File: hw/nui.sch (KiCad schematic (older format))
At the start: 20 parts, among them J1 D_PWR, J2 IR_RCV, J3 A_PWR, J4 Input, J5 Output, U1 Teensy-LC, U2 TC7660S, U3 PGA2311

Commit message: Footprints assigned and created
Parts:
- D1, D2: footprint (none) -> alvarop:SP1002-02JTG
- J4, J5: footprint (none) -> alvarop:SJ-3524-SMT-TR
- U1: footprint (none) -> alvarop:Teensy-LC
- U2: footprint (none) -> alvarop:TC7660S-SOIC
- U3: footprint (none) -> alvarop:PGA2311-SOIC
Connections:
- no-connect marks 19 -> 21
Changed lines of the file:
@@
 LIBS:valves
 LIBS:alvarop
-LIBS:teensy
 LIBS:nui-cache
 EELAYER 25 0
@@
 F 0 "U2" H 8450 2300 60  0000 C CNN
 F 1 "TC7660S" H 8450 1800 60  0000 C CNN
-F 2 "" H 8450 2050 60  0001 C CNN
+F 2 "alvarop:TC7660S-SOIC" H 8450 2050 60  0001 C CNN
 F 3 "" H 8450 2050 60  0001 C CNN
 F 4 " TC7660SEOA713" H 8450 2050 60  0001 C CNN "MPN"
@@
 F 0 "U3" H 8450 4600 60  0000 C CNN
 F 1 "PGA2311" H 8450 3700 60  0000 C CNN
-F 2 "" H 8450 4150 60  0001 C CNN
+F 2 "alvarop:PGA2311-SOIC" H 8450 4150 60  0001 C CNN
 F 3 "" H 8450 4150 60  0001 C CNN
 F 4 "PGA2311U" H 8450 4150 60  0001 C CNN "MPN"
@@
 F 0 "J5" H 8750 5190 50  0000 C CNN
 F 1 "Output" H 8600 4800 50  0000 L CNN
-F 2 "" H 9000 5100 50  0001 C CNN
+F 2 "alvarop:SJ-3524-SMT-TR" H 9000 5100 50  0001 C CNN
 F 3 "" H 9000 5100 50  0001 C CNN
 F 4 " SJ-3524-SMT-TR" H 8750 5000 60  0001 C CNN "MPN"
@@
 	7150 3200 7150 3150
 Wire Wire Line
-	7150 3150 7450 3150
-Wire Wire Line
-	7450 3150 7650 3150
+	7150 3150 7650 3150
 Wire Wire Line
 	7450 3200 7450 3150
@@
 	7150 3400 7150 3450
 Wire Wire Line
-	7150 3450 7450 3450
-Wire Wire Line
-	7450 3450 7650 3450
+	7150 3450 7650 3450
 Wire Wire Line
 	7450 3400 7450 3450
@@
 	8150 3200 8150 3150
 Wire Wire Line
-	8150 3150 8450 3150
-Wire Wire Line
-	8450 3150 8650 3150
+	8150 3150 8650 3150
 Wire Wire Line
 	8450 3200 8450 3150
@@
 	8150 3400 8150 3450
 Wire Wire Line
-	8150 3450 8450 3450
-Wire Wire Line
-	8450 3450 8650 3450
+	8150 3450 8650 3450
 Wire Wire Line
 	8450 3400 8450 3450
@@
 	9100 3200 9100 3150
 Wire Wire Line
-	9100 3150 9400 3150
-Wire Wire Line
-	9400 3150 9600 3150
+	9100 3150 9600 3150
 Wire Wire Line
 	9400 3200 9400 3150
@@
 	9100 3400 9100 3450
 Wire Wire Line
-	9100 3450 9400 3450
-Wire Wire Line
-	9400 3450 9600 3450
+	9100 3450 9600 3450
 Wire Wire Line
 	9400 3400 9400 3450
 Connection ~ 9400 3450
 Wire Wire Line
-	8800 1900 8850 1900
-Wire Wire Line
-	8850 1900 9000 1900
-Wire Wire Line
-	9000 1900 9200 1900
-Wire Wire Line
-	9200 1900 9450 1900
+	8800 1900 9450 1900
 Wire Wire Line
 	8850 1900 8850 1650
@@
 Connection ~ 8850 1900
 Wire Wire Line
-	8800 2200 9000 2200
-Wire Wire Line
-	9000 2200 9200 2200
-Wire Wire Line
-	9200 2200 9450 2200
+	8800 2200 9450 2200
 Wire Wire Line
 	7200 1950 7200 1900
 Wire Wire Line
-	7200 1900 7400 1900
-Wire Wire Line
-	7400 1900 7950 1900
+	7200 1900 7950 1900
 Wire Wire Line
 	7950 1900 7950 2000
@@
 Connection ~ 7400 1900
 Wire Wire Line
-	7200 2200 7400 2200
-Wire Wire Line
-	7400 2200 7500 2200
+	7200 2200 7500 2200
 Wire Wire Line
 	7400 2200 7400 2150
@@
 Wire Wire Line
 	3500 2750 3350 2750
-Wire Wire Line
-	3500 2650 3350 2650
-Wire Wire Line
-	3500 2550 3350 2550
 Text Label 3350 2850 2    60   ~ 0
 MUTE_N
@@
 $EndComp
 Wire Wire Line
-	8550 5200 8550 5350
-Wire Wire Line
-	8550 5350 8550 5450
-Wire Wire Line
-	8550 5450 8550 5550
-Wire Wire Line
-	8950 5100 9350 5100
-Wire Wire Line
-	9350 5100 9450 5100
-Wire Wire Line
-	8950 4900 9250 4900
-Wire Wire Line
-	9250 4900 9450 4900
+	8550 5200 8550 5550
+Wire Wire Line
+	8950 5100 9450 5100
+Wire Wire Line
+	8950 4900 9450 4900
 Text Label 8050 5100 0    60   ~ 0
 VIN_L
@@
 F 0 "D2" H 9000 5550 60  0000 C CNN
 F 1 "SP1002-02JTG" H 9000 5240 60  0000 C CNN
-F 2 "" H 8880 5230 60  0001 C CNN
+F 2 "alvarop:SP1002-02JTG" H 8880 5230 60  0001 C CNN
 F 3 "" H 8880 5230 60  0001 C CNN
 F 4 " SP1002-02JTG" H 9000 5400 60  0001 C CNN "MPN"
@@
 F 0 "J4" H 7350 5190 50  0000 C CNN
 F 1 "Input" H 7200 4800 50  0000 L CNN
-F 2 "" H 7600 5100 50  0001 C CNN
+F 2 "alvarop:SJ-3524-SMT-TR" H 7600 5100 50  0001 C CNN
 F 3 "" H 7600 5100 50  0001 C CNN
 F 4 " SJ-3524-SMT-TR" H 7350 5000 60  0001 C CNN "MPN"
@@
 $EndComp
 Wire Wire Line
-	7150 5200 7150 5350
-Wire Wire Line
-	7150 5350 7150 5450
-Wire Wire Line
-	7150 5450 7150 5550
-Wire Wire Line
-	7550 5100 7950 5100
-Wire Wire Line
-	7950 5100 8050 5100
-Wire Wire Line
-	7550 4900 7850 4900
-Wire Wire Line
-	7850 4900 8050 4900
+	7150 5200 7150 5550
+Wire Wire Line
+	7550 5100 8050 5100
+Wire Wire Line
+	7550 4900 8050 4900
 NoConn ~ 7550 5000
 Wire Wire Line
@@
 F 0 "D1" H 7600 5550 60  0000 C CNN
 F 1 "SP1002-02JTG" H 7600 5240 60  0000 C CNN
-F 2 "" H 7480 5230 60  0001 C CNN
+F 2 "alvarop:SP1002-02JTG" H 7480 5230 60  0001 C CNN
 F 3 "" H 7480 5230 60  0001 C CNN
 F 4 " SP1002-02JTG" H 7600 5400 60  0001 C CNN "MPN"
@@
 F 0 "U1" H 4550 3650 60  0000 C CNN
 F 1 "Teensy-LC" H 4550 1650 60  0000 C CNN
-F 2 "" H 4550 1950 60  0001 C CNN
+F 2 "alvarop:Teensy-LC" H 4550 1950 60  0001 C CNN
 F 3 "" H 4550 1950 60  0000 C CNN
 F 4 "TEENSYLC" H 4550 2500 60  0001 C CNN "MPN"
@@
 $EndComp
 NoConn ~ 5650 2550
+NoConn ~ 3500 2550
+NoConn ~ 3500 2650
+$Comp
+L PWR_FLAG #FLG020
+U 1 1 5A4A9E01
+P 3650 6700
+F 0 "#FLG020" H 3650 6775 50  0001 C CNN
+F 1 "PWR_FLAG" H 3650 6850 50  0000 C CNN
+F 2 "" H 3650 6700 50  0001 C CNN
+F 3 "" H 3650 6700 50  0001 C CNN
+	1    3650 6700
+	1    0    0    -1
+$EndComp
+Connection ~ 3650 6700
+$Comp
+L PWR_FLAG #FLG021
+U 1 1 5A4A9ED3
+P 4650 6750
+F 0 "#FLG021" H 4650 6825 50  0001 C CNN
+F 1 "PWR_FLAG" H 4650 6900 50  0000 C CNN
+F 2 "" H 4650 6750 50  0001 C CNN
+F 3 "" H 4650 6750 50  0001 C CNN
+	1    4650 6750
+	1    0    0    -1
+$EndComp
+$Comp
+L PWR_FLAG #FLG022
+U 1 1 5A4A9F42
+P 5750 6750
+F 0 "#FLG022" H 5750 6825 50  0001 C CNN
+F 1 "PWR_FLAG" H 5750 6900 50  0000 C CNN
+F 2 "" H 5750 6750 50  0001 C CNN
+F 3 "" H 5750 6750 50  0001 C CNN
+	1    5750 6750
+	1    0    0    -1
+$EndComp
+$Comp
+L PWR_FLAG #FLG023
+U 1 1 5A4A9F89
+P 5750 6950
+F 0 "#FLG023" H 5750 7025 50  0001 C CNN
+F 1 "PWR_FLAG" H 5750 7100 50  0000 C CNN
+F 2 "" H 5750 6950 50  0001 C CNN
+F 3 "" H 5750 6950 50  0001 C CNN
+	1    5750 6950
+	-1   0    0    1
+$EndComp
+Connection ~ 4650 6750
+Connection ~ 5750 6750
+Connection ~ 5750 6950
+$Comp
+L PWR_FLAG #FLG?
+U 1 1 5A4AA207
+P 6000 2050
+F 0 "#FLG?" H 6000 2125 50  0001 C CNN
+F 1 "PWR_FLAG" H 6000 2200 50  0000 C CNN
+F 2 "" H 6000 2050 50  0001 C CNN
+F 3 "" H 6000 2050 50  0001 C CNN
+	1    6000 2050
+	-1   0    0    1
+$EndComp
+Connection ~ 6000 2050
 $EndSCHEMATC

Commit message: Layout almost done
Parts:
- removed C2, C7: DNP, Capacitors_Tantalum_SMD:CP_Tantalum_Case-A_EIA-3216-18_Reflow, symbol CP1_Small
- added R1, R2: 0, Capacitors_SMD:C_0603, symbol R_Small
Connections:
- net GNDA: now also C9.1, R1.1; no longer C1.2, C4.2, J1.2 (Pin_2), J2.3 (Pin_3), U1.1 (GND), U1.27 (GND), U3.5 (DGND)
- net IR_IN: now also U1.23 (21_A7_MOSI1_RX1); no longer U1.4 (2)
- net VA_P: now also R2.1; no longer C9.1
- net VD_P: now also R2.2
- net VIN_L: now also D1.5; no longer D1.4
- net VIN_R: now also D1.4; no longer D1.5
- net VOUT_L: now also D2.5; no longer D2.4
- net VOUT_R: now also D2.4; no longer D2.5
- new net GNDD: C1.2, C4.2, J1.2 (Pin_2), J2.3 (Pin_3), R1.2, U1.1 (GND), U1.27 (GND), U3.5 (DGND)
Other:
- moved on the sheet: C3, C9, J1, J3, U2

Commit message: Layout done for v0.0.1
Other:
- moved on the sheet: R2
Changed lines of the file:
@@
 Sheet 1 1
 Title "Nui"
-Date "2017-12-31"
+Date "2018-01-01"
 Rev "0.0.1"
 Comp "Alvaro Prieto"
@@
 $EndComp
 $Comp
-L GNDA #PWR2
+L GNDA #PWR01
 U 1 1 5A49516A
 P 3800 5400
-F 0 "#PWR2" H 3800 5150 50  0001 C CNN
+F 0 "#PWR01" H 3800 5150 50  0001 C CNN
 F 1 "GNDA" H 3800 5250 50  0000 C CNN
 F 2 "" H 3800 5400 50  0001 C CNN
@@
 $EndComp
 $Comp
-L GNDD #PWR3
+L GNDD #PWR02
 U 1 1 5A4951A6
 P 4200 5400
-F 0 "#PWR3" H 4200 5150 50  0001 C CNN
+F 0 "#PWR02" H 4200 5150 50  0001 C CNN
 F 1 "GNDD" H 4200 5275 50  0000 C CNN
 F 2 "" H 4200 5400 50  0001 C CNN
@@
 VIN_R
 $Comp
-L GNDA #PWR18
+L GNDA #PWR03
 U 1 1 5A495347
 P 9450 3950
-F 0 "#PWR18" H 9450 3700 50  0001 C CNN
+F 0 "#PWR03" H 9450 3700 50  0001 C CNN
 F 1 "GNDA" H 9450 3800 50  0000 C CNN
 F 2 "" H 9450 3950 50  0001 C CNN
@@
 $EndComp
 $Comp
-L GNDA #PWR19
+L GNDA #PWR04
 U 1 1 5A49536A
 P 9450 4450
-F 0 "#PWR19" H 9450 4200 50  0001 C CNN
+F 0 "#PWR04" H 9450 4200 50  0001 C CNN
 F 1 "GNDA" H 9450 4300 50  0000 C CNN
 F 2 "" H 9450 4450 50  0001 C CNN
@@
 $EndComp
 $Comp
-L GNDD #PWR12
+L GNDD #PWR05
 U 1 1 5A495395
 P 7350 4250
-F 0 "#PWR12" H 7350 4000 50  0001 C CNN
+F 0 "#PWR05" H 7350 4000 50  0001 C CNN
 F 1 "GNDD" H 7350 4125 50  0000 C CNN
 F 2 "" H 7350 4250 50  0001 C CNN
@@
 VA_P
 $Comp
-L GNDA #PWR16
+L GNDA #PWR06
 U 1 1 5A495C3B
 P 8650 3450
-F 0 "#PWR16" H 8650 3200 50  0001 C CNN
+F 0 "#PWR06" H 8650 3200 50  0001 C CNN
 F 1 "GNDA" H 8650 3300 50  0000 C CNN
 F 2 "" H 8650 3450 50  0001 C CNN
@@
 VA_M
 $Comp
-L GNDA #PWR20
+L GNDA #PWR07
 U 1 1 5A495C94
 P 9600 3150
-F 0 "#PWR20" H 9600 2900 50  0001 C CNN
+F 0 "#PWR07" H 9600 2900 50  0001 C CNN
 F 1 "GNDA" H 9600 3000 50  0000 C CNN
 F 2 "" H 9600 3150 50  0001 C CNN
@@
 $EndComp
 $Comp
-L GNDD #PWR13
+L GNDD #PWR08
 U 1 1 5A495D69
 P 7650 3450
-F 0 "#PWR13" H 7650 3200 50  0001 C CNN
+F 0 "#PWR08" H 7650 3200 50  0001 C CNN
 F 1 "GNDD" H 7650 3325 50  0000 C CNN
 F 2 "" H 7650 3450 50  0001 C CNN
@@
 VA_P
 $Comp
-L GNDA #PWR14
+L GNDA #PWR09
 U 1 1 5A496296
 P 7700 2050
-F 0 "#PWR14" H 7700 1800 50  0001 C CNN
+F 0 "#PWR09" H 7700 1800 50  0001 C CNN
 F 1 "GNDA" H 7700 1900 50  0000 C CNN
 F 2 "" H 7700 2050 50  0001 C CNN
@@
 $EndComp
 $Comp
-L GNDD #PWR1
+L GNDD #PWR010
 U 1 1 5A496F6F
 P 2750 1900
-F 0 "#PWR1" H 2750 1650 50  0001 C CNN
+F 0 "#PWR010" H 2750 1650 50  0001 C CNN
 F 1 "GNDD" H 2750 1775 50  0000 C CNN
 F 2 "" H 2750 1900 50  0001 C CNN
@@
 VD_P
 $Comp
-L GNDD #PWR9
+L GNDD #PWR011
 U 1 1 5A497AF2
 P 6550 2000
-F 0 "#PWR9" H 6550 1750 50  0001 C CNN
+F 0 "#PWR011" H 6550 1750 50  0001 C CNN
 F 1 "GNDD" H 6550 1875 50  0000 C CNN
 F 2 "" H 6550 2000 50  0001 C CNN
@@
 $EndComp
 $Comp
-L +3V3 #PWR7
+L +3V3 #PWR012
 U 1 1 5A497CF0
 P 6050 2050
-F 0 "#PWR7" H 6050 1900 50  0001 C CNN
+F 0 "#PWR012" H 6050 1900 50  0001 C CNN
 F 1 "+3V3" H 6050 2190 50  0000 C CNN
 F 2 "" H 6050 2050 50  0001 C CNN
@@
 IR_IN
 $Comp
-L GNDD #PWR8
+L GNDD #PWR013
 U 1 1 5A4983FA
 P 6200 4100
-F 0 "#PWR8" H 6200 3850 50  0001 C CNN
+F 0 "#PWR013" H 6200 3850 50  0001 C CNN
 F 1 "GNDD" H 6200 3975 50  0000 C CNN
 F 2 "" H 6200 4100 50  0001 C CNN
@@
 $EndComp
 $Comp
-L +3V3 #PWR6
+L +3V3 #PWR014
 U 1 1 5A498435
 P 6000 4250
-F 0 "#PWR6" H 6000 4100 50  0001 C CNN
+F 0 "#PWR014" H 6000 4100 50  0001 C CNN
 F 1 "+3V3" H 6000 4390 50  0000 C CNN
 F 2 "" H 6000 4250 50  0001 C CNN
@@
 IR_IN
 $Comp
-L GNDA #PWR15
+L GNDA #PWR015
 U 1 1 5A49870F
 P 8550 5550
-F 0 "#PWR15" H 8550 5300 50  0001 C CNN
+F 0 "#PWR015" H 8550 5300 50  0001 C CNN
 F 1 "GNDA" H 8550 5400 50  0000 C CNN
 F 2 "" H 8550 5550 50  0001 C CNN
@@
 VA_M
 $Comp
-L GNDA #PWR10
+L GNDA #PWR016
 U 1 1 5A499932
 P 6550 5600
-F 0 "#PWR10" H 6550 5350 50  0001 C CNN
+F 0 "#PWR016" H 6550 5350 50  0001 C CNN
 F 1 "GNDA" H 6550 5450 50  0000 C CNN
 F 2 "" H 6550 5600 50  0001 C CNN
@@
 VD_P
 $Comp
-L GNDD #PWR5
+L GNDD #PWR017
 U 1 1 5A499BC6
 P 5450 5600
-F 0 "#PWR5" H 5450 5350 50  0001 C CNN
+F 0 "#PWR017" H 5450 5350 50  0001 C CNN
 F 1 "GNDD" H 5450 5475 50  0000 C CNN
 F 2 "" H 5450 5600 50  0001 C CNN
@@
 $EndComp
 $Comp
-L +3V3 #PWR4
+L +3V3 #PWR018
 U 1 1 5A499C74
 P 5100 5650
-F 0 "#PWR4" H 5100 5500 50  0001 C CNN
+F 0 "#PWR018" H 5100 5500 50  0001 C CNN
 F 1 "+3V3" H 5100 5790 50  0000 C CNN
 F 2 "" H 5100 5650 50  0001 C CNN
@@
 $EndComp
 $Comp
-L GNDA #PWR11
+L GNDA #PWR019
 U 1 1 5A49C834
 P 7150 5550
-F 0 "#PWR11" H 7150 5300 50  0001 C CNN
+F 0 "#PWR019" H 7150 5300 50  0001 C CNN
 F 1 "GNDA" H 7150 5400 50  0000 C CNN
 F 2 "" H 7150 5550 50  0001 C CNN
@@
 U 1 1 5A496E83
 P 4550 2500
-F 0 "U1" H 4550 3650 60  0000 C CNN
+F 0 "U1" H 4550 3350 60  0000 C CNN
 F 1 "Teensy-LC" H 4550 1650 60  0000 C CNN
 F 2 "alvarop:Teensy-LC" H 4550 1950 60  0001 C CNN
@@
 NoConn ~ 3500 2650
 $Comp
-L PWR_FLAG #FLG1
+L PWR_FLAG #FLG020
 U 1 1 5A4A9ED3
 P 5050 5450
-F 0 "#FLG1" H 5050 5525 50  0001 C CNN
+F 0 "#FLG020" H 5050 5525 50  0001 C CNN
 F 1 "PWR_FLAG" H 5050 5600 50  0000 C CNN
 F 2 "" H 5050 5450 50  0001 C CNN
@@
 $EndComp
 $Comp
-L PWR_FLAG #FLG3
+L PWR_FLAG #FLG021
 U 1 1 5A4A9F42
 P 6150 5450
-F 0 "#FLG3" H 6150 5525 50  0001 C CNN
+F 0 "#FLG021" H 6150 5525 50  0001 C CNN
 F 1 "PWR_FLAG" H 6150 5600 50  0000 C CNN
 F 2 "" H 6150 5450 50  0001 C CNN
@@
 $EndComp
 $Comp
-L PWR_FLAG #FLG4
+L PWR_FLAG #FLG022
 U 1 1 5A4A9F89
 P 6150 5650
-F 0 "#FLG4" H 6150 5725 50  0001 C CNN
+F 0 "#FLG022" H 6150 5725 50  0001 C CNN
 F 1 "PWR_FLAG" H 6150 5800 50  0000 C CNN
 F 2 "" H 6150 5650 50  0001 C CNN
@@
 $EndComp
 $Comp
-L PWR_FLAG #FLG2
+L PWR_FLAG #FLG023
 U 1 1 5A4AA207
 P 6000 2050
-F 0 "#FLG2" H 6000 2125 50  0001 C CNN
+F 0 "#FLG023" H 6000 2125 50  0001 C CNN
 F 1 "PWR_FLAG" H 6000 2200 50  0000 C CNN
 F 2 "" H 6000 2050 50  0001 C CNN
@@
 	7400 1800 7950 1800
 $Comp
-L GNDA #PWR17
+L GNDA #PWR024
 U 1 1 5A4AB659
 P 9200 2350
-F 0 "#PWR17" H 9200 2100 50  0001 C CNN
+F 0 "#PWR024" H 9200 2100 50  0001 C CNN
 F 1 "GNDA" H 9200 2200 50  0000 C CNN
 F 2 "" H 9200 2350 50  0001 C CNN
@@
 L R_Small R2
 U 1 1 5A4AC5D1
-P 4000 4800
-F 0 "R2" H 4030 4820 50  0000 L CNN
-F 1 "0" H 4030 4760 50  0000 L CNN
-F 2 "Capacitors_SMD:C_0603" H 4000 4800 50  0001 C CNN
-F 3 "" H 4000 4800 50  0001 C CNN
-	1    4000 4800
+P 4000 5050
+F 0 "R2" H 4030 5070 50  0000 L CNN
+F 1 "0" H 4030 5010 50  0000 L CNN
+F 2 "Capacitors_SMD:C_0603" H 4000 5050 50  0001 C CNN
+F 3 "" H 4000 5050 50  0001 C CNN
+	1    4000 5050
 	0    -1   -1   0
 $EndComp
 Wire Wire Line
-	3900 4800 3800 4800
-Wire Wire Line
-	4100 4800 4200 4800
-Text Label 3800 4800 2    60   ~ 0
+	3900 5050 3800 5050
+Wire Wire Line
+	4100 5050 4200 5050
+Text Label 3800 5050 2    60   ~ 0
 VA_P
-Text Label 4200 4800 0    60   ~ 0
+Text Label 4200 5050 0    60   ~ 0
 VD_P
 Wire Wire Line

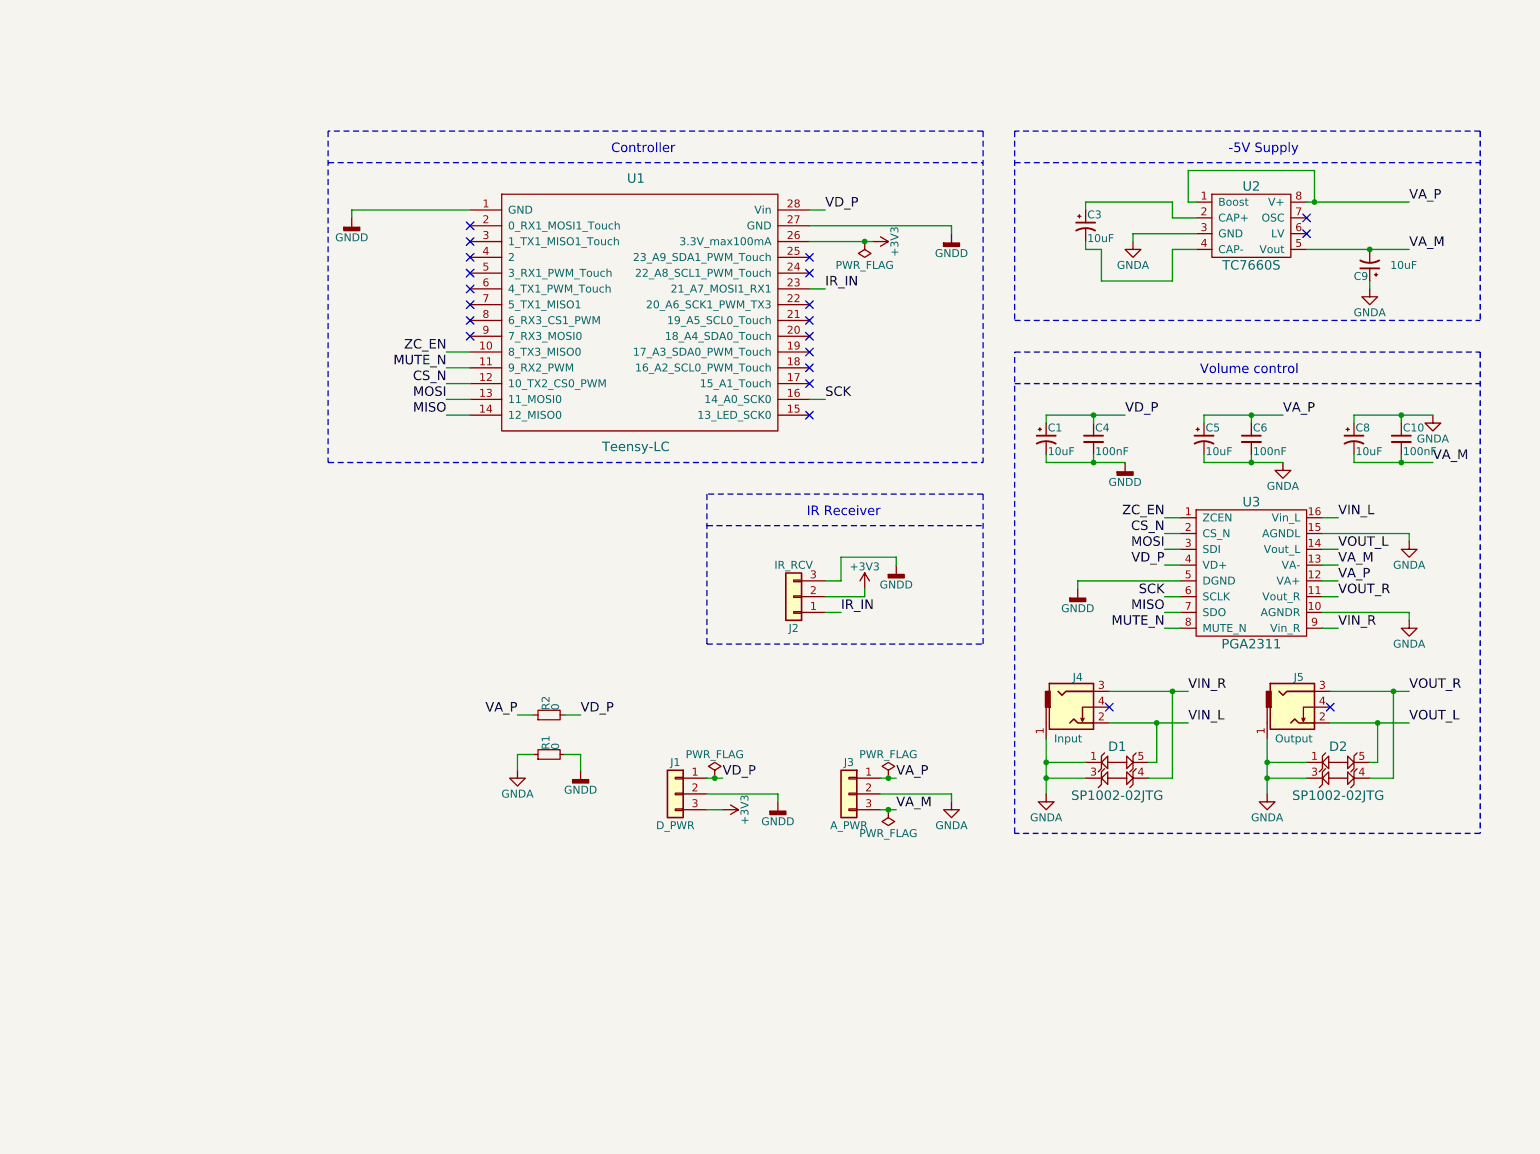
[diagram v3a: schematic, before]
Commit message: Updating power supply circuit in NUI
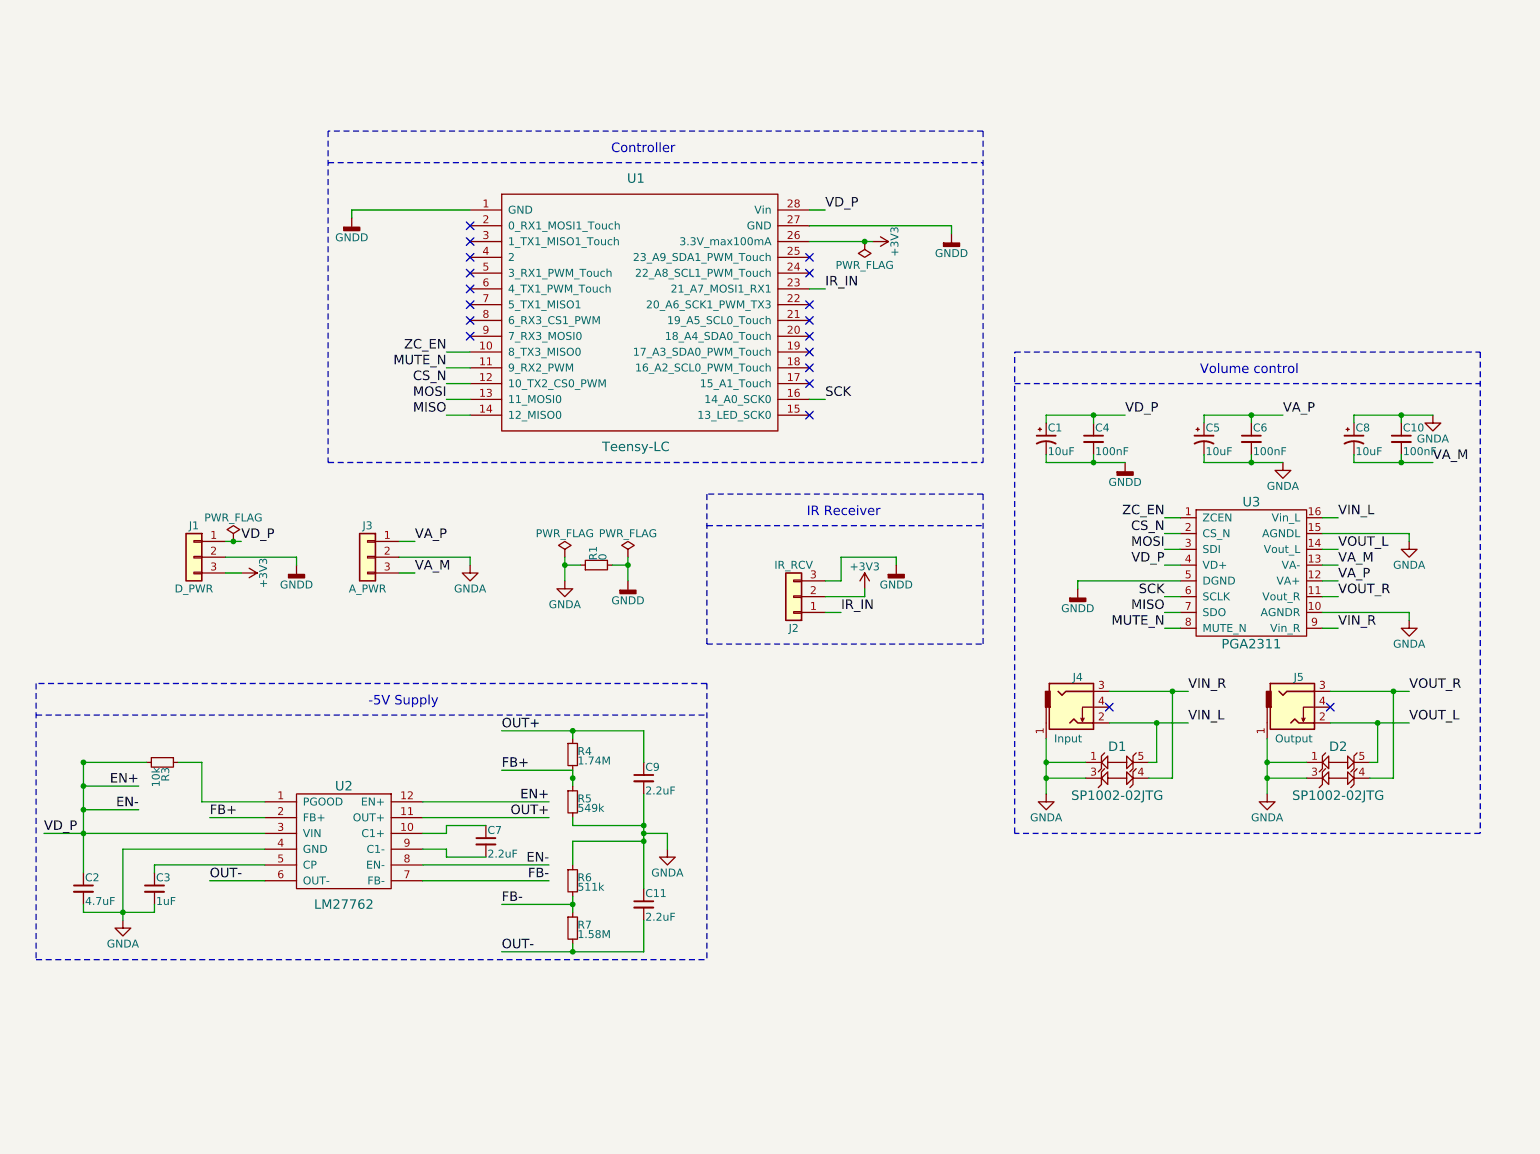
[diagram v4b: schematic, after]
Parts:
- removed C3, C9: 10uF, Capacitors_SMD:CP_Elec_4x5.3, symbol CP1_Small
- removed R2: 0, Capacitors_SMD:C_0603, symbol R_Small
- removed U2: TC7660S, alvarop:TC7660S-SOIC, symbol TC7660S
- added C11, C7, C9: 2.2uF, symbol C_Small
- added C2: 4.7uF, symbol C_Small
- added C3: 1uF, symbol C_Small
- added R3: 10k, symbol R_Small
- added R4: 1.74M, symbol R_Small
- added R5: 549k, symbol R_Small
- added R6: 511k, symbol R_Small
- added R7: 1.58M, symbol R_Small
- added U2: LM27762, symbol LM27762
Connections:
- net GNDA: now also C11.1, C2.2, C3.2, C9.2, R5.2, R6.1, U2.4 (GND)
- net VD_P renamed EN+
- net EN+: now also C2.1, R3.2, U2.12 (EN+), U2.3 (VIN), U2.8 (EN-)
- new net: R3.1, U2.1 (PGOOD)
- new net: C7.1, U2.10 (C1+)
- new net: C3.1, U2.5 (CP)
- new net: C7.2, U2.9 (C1-)
- new net FB+: R4.2, R5.1, U2.2 (FB+)
- new net FB-: R6.2, R7.1, U2.7 (FB-)
- new net OUT+: C9.1, R4.1, U2.11 (OUT+)
- new net OUT-: C11.2, R7.2, U2.6 (OUT-)
- no-connect marks 21 -> 19
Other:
- moved on the sheet: J1, J3, R1
